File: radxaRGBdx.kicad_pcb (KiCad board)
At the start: 2 copper layers, 65 x 30 mm, 69 parts, among them J1 Conn_02x20_Odd_Even

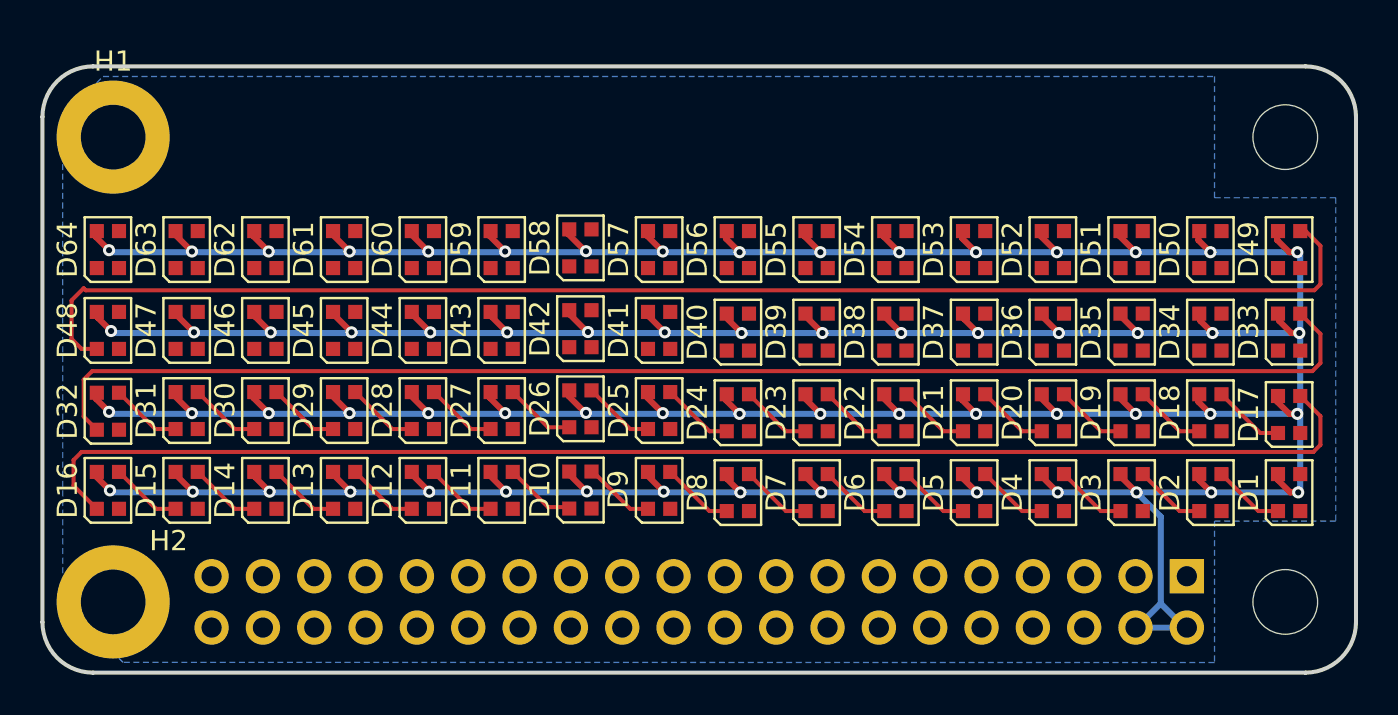
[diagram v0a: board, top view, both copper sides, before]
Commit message: Routing work, added level shifters / MCU / IMU, routed power / signals
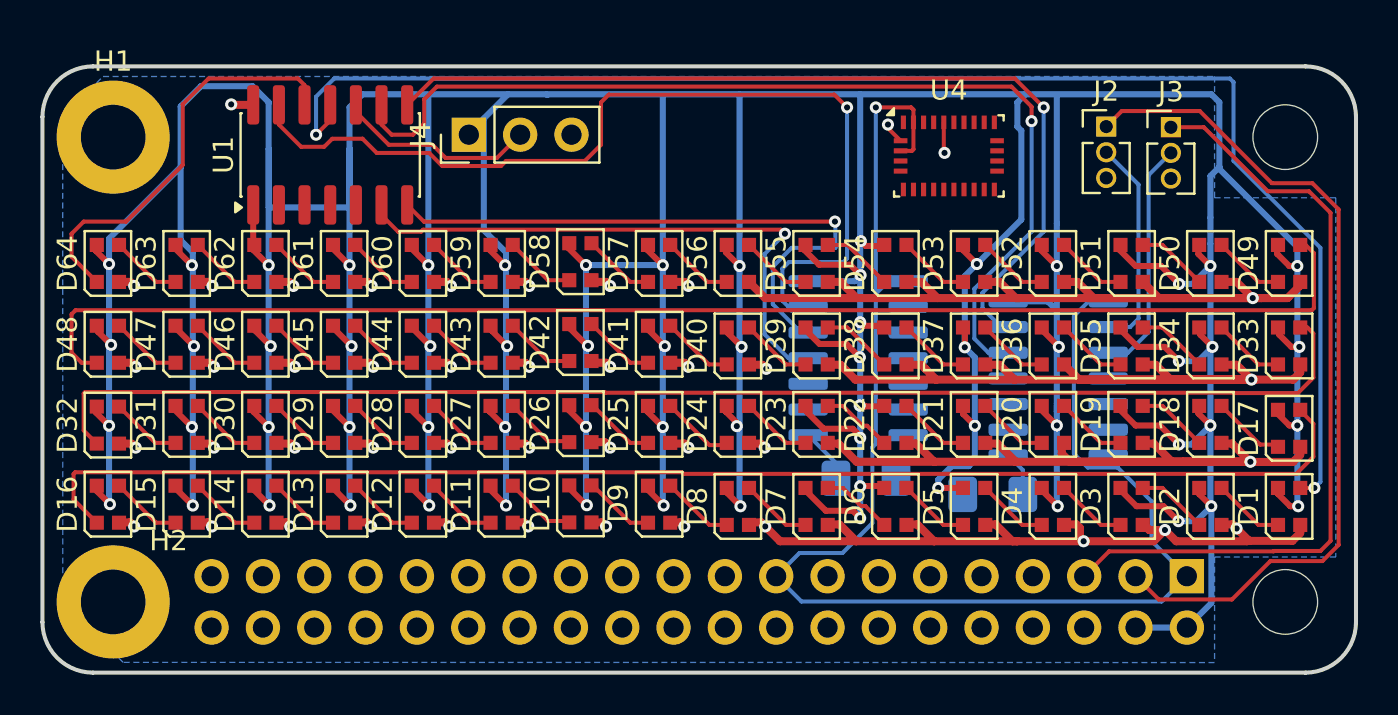
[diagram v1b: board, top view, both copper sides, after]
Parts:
- added J2: JMP_I2C_SDA, Connector_PinHeader_1.27mm:PinHeader_1x03_P1.27mm_Vertical, F.Cu at (152.9, 78.0)
- added J3: JMP_I2C_SCL, Connector_PinHeader_1.27mm:PinHeader_1x03_P1.27mm_Vertical, F.Cu at (156.1, 78.0)
- added J4: ATTINY_UDPI, Connector_PinHeader_2.54mm:PinHeader_1x03_P2.54mm_Vertical, F.Cu at (121.4, 78.4)
- added R1: 110k, PCM_Resistor_SMD_AKL:R_1206_3216Metric_Pad1.42x1.75mm_HandSolder, B.Cu at (147.3, 96.2)
- added R2: 110k, PCM_Resistor_SMD_AKL:R_1206_3216Metric_Pad1.42x1.75mm_HandSolder, B.Cu at (141.0, 95.4)
- added U1: ATtiny1614-SS, Package_SO:SOIC-14_3.9x8.7mm_P1.27mm, F.Cu at (114.5, 79.4)
- added U2: TXB0104D, Package_SO:SOIC-14_3.9x8.7mm_P1.27mm, B.Cu at (150.5, 90.5)
- added U3: TXB0104D, Package_SO:SOIC-14_3.9x8.7mm_P1.27mm, B.Cu at (140.6, 89.5)
- added U4: BNO055, Package_LGA:LGA-28_5.2x3.8mm_P0.5mm, F.Cu at (145.1, 79.5)
- moved D26 0.73 mm to (126.9, 92.7)
- moved D1 0.69 mm to (161.9, 96.8)
- moved D10 0.69 mm to (126.9, 96.7)
- moved D11 0.69 mm to (123.0, 96.7)
- moved D12 0.69 mm to (119.1, 96.7)
- moved D13 0.69 mm to (115.2, 96.7)
- moved D14 0.69 mm to (111.3, 96.7)
- moved D15 0.69 mm to (107.4, 96.7)
- moved D16 0.69 mm to (103.5, 96.7)
- moved D17 0.69 mm to (161.9, 92.9)
- moved D2 0.69 mm to (158.1, 96.8)
- moved D25 0.69 mm to (130.8, 92.7)
- moved D27 0.69 mm to (123.0, 92.7)
- moved D28 0.69 mm to (119.1, 92.7)
- moved D29 0.69 mm to (115.2, 92.7)
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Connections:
- J1 pad 1: unconnected-(J1-Pin_1-Pad1) -> +3V3
- J1 pad 17: unconnected-(J1-Pin_17-Pad17) -> +3V3
- J1 pad 29: unconnected-(J1-Pin_29-Pad29) -> /RDX_I2C_SCL
- J1 pad 3: unconnected-(J1-Pin_3-Pad3) -> /RPI_I2C_SDA
- J1 pad 31: unconnected-(J1-Pin_31-Pad31) -> /RDX_I2C_SDA
- J1 pad 5: unconnected-(J1-Pin_5-Pad5) -> /RPI_I2C_SCL
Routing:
- net GND: track 0.00 -> 210.0 mm, vias 0 -> 44
- net VCC: track 341.6 -> 462.0 mm
- net +3V3: track 0.00 -> 72.3 mm, vias 0 -> 1
- net /RGB_DIN: track 0.00 -> 72.2 mm, vias 0 -> 2
- net /I2C_SCL_5: track 0.00 -> 50.1 mm, vias 0 -> 1
- net /IMU_SPI_CLK_5: track 0.00 -> 47.1 mm, vias 0 -> 1
- net /I2C_SDA_5: track 0.00 -> 45.5 mm, vias 0 -> 1
- net /RPI_I2C_SDA: track 0.00 -> 42.1 mm
- net /RPI_I2C_SCL: track 0.00 -> 38.8 mm
- net /IMU_SPI_MOSI_5: track 0.00 -> 30.5 mm, vias 0 -> 1
- net /IMU_SPI_MISO_5: track 0.00 -> 29.0 mm, vias 0 -> 1
- net /RGB_DOUT: track 0.00 -> 20.5 mm
- net /I2C_SCL: track 0.00 -> 11.7 mm
- net /I2C_SDA: track 0.00 -> 10.6 mm
- net /UDPI_IN: track 0.00 -> 9.90 mm
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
